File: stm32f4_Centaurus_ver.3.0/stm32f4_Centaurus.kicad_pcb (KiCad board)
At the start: 2 copper layers, 100 x 79 mm, 221 parts, among them IC1 PIC24FJ64GB004, J1 SERIAL1, J2 EXTERNAL_~RST, P1 PICKit3, P10 XA2_12V, P11 CAN0, P12 CAN1, P13 CAN0, P14 CAN1, P15 SERIAL2, P16 SERIAL0, P17 XA2_5V, P18 SWD, P2 SERIAL5_SBDBT, P23 A/D, P24 PWM, P25 A/D_batt, P26 PWM_batt, P27 EMERGENCY_CHECK, P28 I/O_5V, P29 I/O_Variable, P3 ENC0, P30 I/O_5V_batt, P31 I/O_Variable, P4 ENC2, P5 SPI0, P6 ENC3, P7 ENC1, P8 SERIAL4, P9 SERIAL3, Q1 FET_P, Q2 FET_P, Q3 FET_P, Q4 NPN, Q5 NPN, Q6 FET_P, Q7 FET_N, SW1 Main_POWER, SW2 SW1, SW3 SW0, SW4 SW2, SW5 SW3, U1 STM32F407VG, U10 LOGO, U11 TLP4227G-2, U13 LOGO, U2 AZ1086H, U3 MCP2221A, U4 BD9G101G, U5 MAX3051, U6 MAX3051, U7 AQM1602_BL, U8 OSTBABS4C2B, U9 LOGO, X1 8MHz

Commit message: いろいろ修正した(なにやったけ? <-おい)
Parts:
- added Q8: FET_N, Mizz_lib:SOT-23, F.Cu at (145.6, 71.2)
- added R77: 510, Mizz_lib:1608_WP, F.Cu at (146.3, 76.8)
- added R78: 10, Mizz_lib:1608_WP, B.Cu at (117.1, 75.2)
- added R79: 10, Mizz_lib:1608_WP, B.Cu at (117.1, 73.2)
- added R80: 10, Mizz_lib:1608_WP, B.Cu at (114.9, 97.5)
- R76: value 10k -> R_JP; moved to B.Cu
- SP1: footprint Mizz_lib:UGCT7525AN4 -> Mizz_lib:PKLCS1212E4001
- U11: value TLP4227G-2 -> CPC1106N; footprint Package_DIP:DIP-8_W7.62mm_SMDSocket_SmallPads -> Package_SO:SOP-4_3.8x4.1mm_P2.54mm; moved to B.Cu
- moved U11 62.9 mm to (144.3, 76.0), turned to 270 degrees
- moved R76 32.6 mm to (146.4, 68.1), turned to 90 degrees
- moved R64 30.3 mm to (145.6, 73.6), turned to 180 degrees
- moved JP6 3.08 mm to (150.0, 80.2), turned to 270 degrees
- moved SP1 1.25 mm to (80.2, 103.2)
- moved J2 0.45 mm to (140.6, 73.8)
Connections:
- D20 pad 2: +3V3 -> +12V
- D34 pad 1: /PE8 -> /PE12
- JP6 pad 2: Net-(JP6-Pad2) -> /EXTERNAL_~RST~_PIN
- P5 pad 3: /SPI2_MOSI -> Net-(P5-Pad3)
- P5 pad 4: /SPI2_MISO -> Net-(P5-Pad4)
- P5 pad 5: /SPI2_SCK -> Net-(P5-Pad5)
- P5 pad 6: /PE10 -> /PE8
- R17 pad 1: /PE12 -> /PE10
- R64 pad 1: Net-(R64-Pad1) -> Net-(JP6-Pad1)
- R76 pad 1: GND -> Net-(Q8-Pad3)
- R76 pad 2: Net-(R76-Pad2) -> +3V3
- SP1 pad 1: +3V3 -> +12V
- U11 pad 1: Net-(J2-Pad3) -> /ST-LINK_Vdd
- U11 pad 2: Net-(R76-Pad2) -> Net-(R77-Pad2)
- U11 pad 3: /ST-LINK_Vdd -> /~RST
- U11 pad 4: Net-(R64-Pad1) -> /EXTERNAL_~RST~_PIN
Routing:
- net Net-(P5-Pad4): track 0.00 -> 47.5 mm, vias 0 -> 7
- net Net-(P5-Pad3): track 0.00 -> 43.9 mm, vias 0 -> 7
- net Net-(R62-Pad1): track 39.8 -> 0.00 mm, vias 7 -> 0
- net Net-(R64-Pad2): track 39.2 -> 0.00 mm, vias 7 -> 0
- net /~RST: track 67.9 -> 94.8 mm
- net Net-(P5-Pad5): track 0.00 -> 26.5 mm
- net +12V: track 25.9 -> 43.1 mm, vias 2 -> 3
- net /PE12: track 23.3 -> 36.6 mm, vias 3 -> 2
- net /PE15: track 53.0 -> 65.8 mm
- net Net-(JP6-Pad1): track 1.21 -> 11.4 mm, vias 0 -> 1
- net /PE10: track 33.9 -> 42.8 mm, vias 2 -> 4
- net +3V3: track 397.1 -> 389.4 mm, vias 25 -> 23
- net /SWCLK: track 29.1 -> 35.9 mm
- net /EXTERNAL_~RST~_PIN: track 0.00 -> 6.68 mm
- net Net-(R63-Pad2): track 6.31 -> 0.00 mm
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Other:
- board text added: "CS_PE8"
- board text removed: "CS"

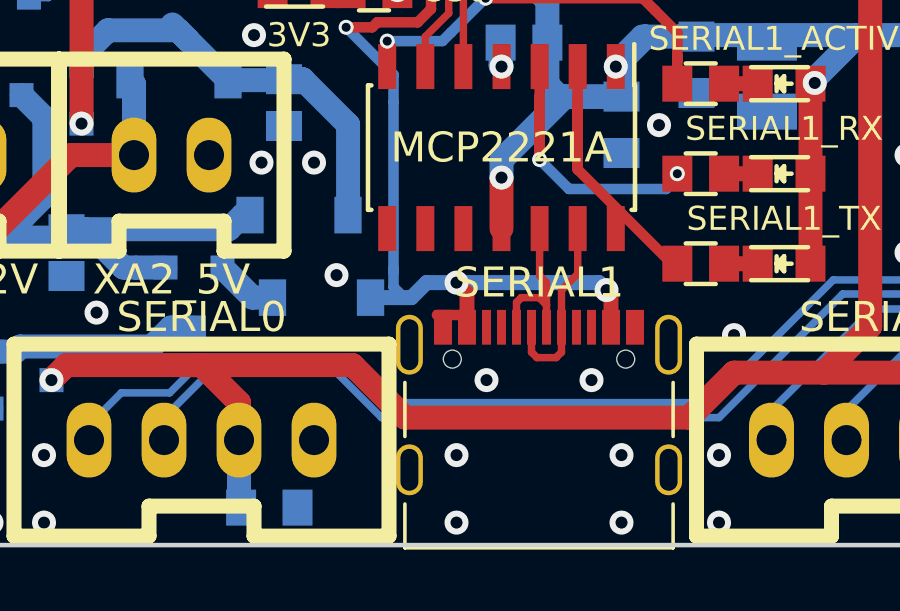
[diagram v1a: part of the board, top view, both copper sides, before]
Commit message: BLDC type2引き終わった，基板にミスがあった
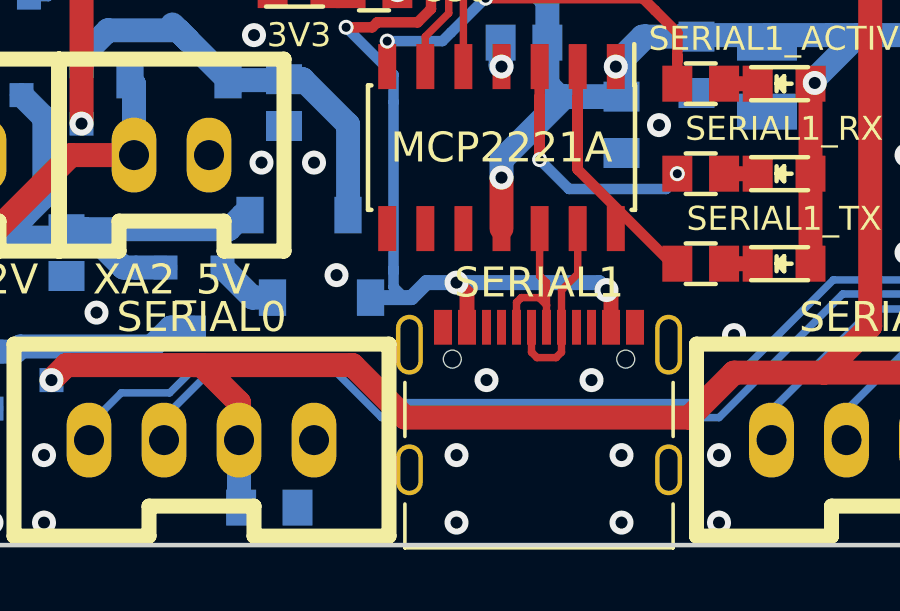
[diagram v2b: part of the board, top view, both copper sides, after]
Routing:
- net /BUS_5V: track 29.3 -> 28.5 mm
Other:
- board text added: "STM32F407VGT6 Board "Centaurus" ver.3.0"
- board text removed: "STM32F407VGT6 Board "Centaurus" ver.2.1.1"

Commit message: またまたミス発見，直した
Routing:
- net Net-(D25-Pad2): track 0.00 -> 0.09 mm, vias 0 -> 1
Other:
- board text added: "11"
- board text removed: "7(RGB,RESET)"
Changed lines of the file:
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@@
     (thickness 1.6)
     (drawings 150)
-    (tracks 2855)
+    (tracks 2857)
     (zones 0)
     (modules 226)
@@
     (effects (font (size 0.8 0.8) (thickness 0.2)) (justify mirror))
   )
-  (gr_text "7(RGB,RESET)" (at 76.5 72.25) (layer B.SilkS)
+  (gr_text 11 (at 76.5 72.25) (layer B.SilkS)
     (effects (font (size 0.8 0.8) (thickness 0.2)) (justify mirror))
   )
@@
   (via (at 112.25 115.63) (size 0.5) (drill 0.3) (layers F.Cu B.Cu) (net 165))
   (segment (start 112.25 115.72) (end 112.25 115.63) (width 0.25) (layer B.Cu) (net 165))
+  (via (at 117.95 115.72) (size 0.5) (drill 0.3) (layers F.Cu B.Cu) (net 166))
+  (segment (start 117.95 115.63) (end 117.95 115.72) (width 0.25) (layer F.Cu) (net 166))
   (segment (start 58.25 73.21) (end 57.29 72.25) (width 0.5) (layer B.Cu) (net 167))
   (segment (start 58.25 81.72) (end 58.25 73.21) (width 0.5) (layer B.Cu) (net 167))

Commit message: 卍配　置　完　了卍
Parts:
- removed Q8: FET_N, Mizz_lib:SOT-23
- added U12: PS7200K-1A, Package_SO:SOP-4_3.8x4.1mm_P2.54mm, B.Cu at (133.2, 74.7)
- R64: moved to B.Cu
- R76: value R_JP -> 330; moved to F.Cu
- moved R76 17.9 mm to (163.8, 72.5), turned to 0 degrees
- moved R64 11.4 mm to (134.4, 71.8)
- moved D40 0.40 mm to (144.2, 71.1)
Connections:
- J2 pad 3: Net-(J2-Pad3) -> /RESET_SIGNAL
- R76 pad 1: Net-(Q8-Pad3) -> GND
- R76 pad 2: +3V3 -> Net-(R76-Pad2)
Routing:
- net Net-(JP6-Pad1): track 11.4 -> 26.3 mm
- net Net-(J2-Pad3): track 5.97 -> 0.00 mm, vias 1 -> 0
- net Net-(Q8-Pad3): track 1.79 -> 0.00 mm, vias 1 -> 0
- net GND: vias 362 -> 360

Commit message: main絶対動くマン
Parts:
- R76: moved to B.Cu
- moved R76 35.6 mm to (128.2, 72.2)
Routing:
- net /RESET_SIGNAL: track 0.00 -> 11.0 mm
- net Net-(R76-Pad2): track 0.00 -> 1.98 mm
- net +3V3: track 389.4 -> 390.7 mm, vias 23 -> 24
- net GND: vias 360 -> 365
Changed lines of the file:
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@@
     (thickness 1.6)
     (drawings 150)
-    (tracks 2857)
+    (tracks 2875)
     (zones 0)
     (modules 226)
@@
       (net 60 "Net-(D20-Pad1)"))
   )
-  (module Mizz_lib:1608_WP (layer F.Cu)
-    (at 163.79 72.5)
+  (module Mizz_lib:1608_WP (layer B.Cu)
+    (at 128.15 72.15)
     (descr <b>CAPACITOR</b>)
-    (fp_text reference R76 (at -0.635 -0.635) (layer F.SilkS) hide
-      (effects (font (size 1.2065 1.2065) (thickness 0.1016)) (justify left bottom))
+    (fp_text reference R76 (at -0.635 0.635) (layer B.SilkS) hide
+      (effects (font (size 1.2065 1.2065) (thickness 0.1016)) (justify right bottom mirror))
     )
-    (fp_text value 330 (at 0 -0.5) (layer F.SilkS)
-      (effects (font (size 0.8 0.8) (thickness 0.15)) (justify bottom))
+    (fp_text value 330 (at -2.7 0.5) (layer B.SilkS)
+      (effects (font (size 0.8 0.8) (thickness 0.15)) (justify bottom mirror))
     )
-    (fp_line (start -0.356 -0.432) (end 0.356 -0.432) (layer Dwgs.User) (width 0.1016))
-    (fp_line (start -0.356 0.419) (end 0.356 0.419) (layer Dwgs.User) (width 0.1016))
-    (fp_poly (pts (xy -0.8382 0.4699) (xy -0.3381 0.4699) (xy -0.3381 -0.4801) (xy -0.8382 -0.4801)) (layer Dwgs.User) (width 0))
-    (fp_poly (pts (xy 0.3302 0.4699) (xy 0.8303 0.4699) (xy 0.8303 -0.4801) (xy 0.3302 -0.4801)) (layer Dwgs.User) (width 0))
-    (fp_poly (pts (xy -0.1999 0.3) (xy 0.1999 0.3) (xy 0.1999 -0.3) (xy -0.1999 -0.3)) (layer F.Adhes) (width 0))
-    (pad 1 smd rect (at -0.9 0) (size 0.8 1) (layers F.Cu F.Paste F.Mask)
+    (fp_line (start -0.356 0.432) (end 0.356 0.432) (layer Dwgs.User) (width 0.1016))
+    (fp_line (start -0.356 -0.419) (end 0.356 -0.419) (layer Dwgs.User) (width 0.1016))
+    (fp_poly (pts (xy -0.8382 -0.4699) (xy -0.3381 -0.4699) (xy -0.3381 0.4801) (xy -0.8382 0.4801)) (layer Dwgs.User) (width 0))
+    (fp_poly (pts (xy 0.3302 -0.4699) (xy 0.8303 -0.4699) (xy 0.8303 0.4801) (xy 0.3302 0.4801)) (layer Dwgs.User) (width 0))
+    (fp_poly (pts (xy -0.1999 -0.3) (xy 0.1999 -0.3) (xy 0.1999 0.3) (xy -0.1999 0.3)) (layer B.Adhes) (width 0))
+    (pad 1 smd rect (at -0.9 0) (size 0.8 1) (layers B.Cu B.Paste B.Mask)
       (net 2 GND))
-    (pad 2 smd rect (at 0.9 0) (size 0.8 1) (layers F.Cu F.Paste F.Mask)
+    (pad 2 smd rect (at 0.9 0) (size 0.8 1) (layers B.Cu B.Paste B.Mask)
       (net 230 "Net-(R76-Pad2)"))
     (model ${KISYS3DMOD}/Resistor_SMD.3dshapes/R_0603_1608Metric.step
@@
   (via (at 141.25 132.25) (size 0.8) (drill 0.4) (layers F.Cu B.Cu) (net 2))
   (via (at 137.5 82.75) (size 0.8) (drill 0.4) (layers F.Cu B.Cu) (net 2))
-  (via (at 137.75 75) (size 0.8) (drill 0.4) (layers F.Cu B.Cu) (net 2))
   (via (at 144.675 74.575) (size 0.5) (drill 0.3) (layers F.Cu B.Cu) (net 2))
   (via (at 140.6 81.175) (size 0.8) (drill 0.4) (layers F.Cu B.Cu) (net 2))
@@
   (via (at 112.85 103.65) (size 0.8) (drill 0.4) (layers F.Cu B.Cu) (net 2))
   (via (at 110.6 107.4) (size 0.8) (drill 0.4) (layers F.Cu B.Cu) (net 2))
+  (via (at 137.7 75.1) (size 0.8) (drill 0.4) (layers F.Cu B.Cu) (net 2))
+  (via (at 134.95 76.7) (size 0.8) (drill 0.4) (layers F.Cu B.Cu) (net 2))
+  (via (at 132.85 69.95) (size 0.5) (drill 0.3) (layers F.Cu B.Cu) (net 2))
+  (via (at 134.25 70.45) (size 0.5) (drill 0.3) (layers F.Cu B.Cu) (net 2))
+  (via (at 134.8 72.85) (size 0.8) (drill 0.4) (layers F.Cu B.Cu) (net 2))
+  (via (at 134.8 75.05) (size 0.8) (drill 0.4) (layers F.Cu B.Cu) (net 2))
   (segment (start 149.42 124.21) (end 148.49 124.21) (width 0.25) (layer B.Cu) (net 3))
   (segment (start 148.49 124.21) (end 148.275001 124.424999) (width 0.25) (layer B.Cu) (net 3))
@@
   (via (at 137 71.75) (size 0.8) (drill 0.4) (layers F.Cu B.Cu) (net 212))
   (segment (start 136.64 72.11) (end 137 71.75) (width 0.8) (layer F.Cu) (net 212))
-  (segment (start 136.64 81.14) (end 136.64 72.11) (width 0.8) (layer F.Cu) (net 212))
   (segment (start 135.83 81.95) (end 136.64 81.14) (width 0.8) (layer F.Cu) (net 212))
   (segment (start 137 71.75) (end 139.915 71.75) (width 0.8) (layer B.Cu) (net 212))
@@
   (segment (start 146.04 66.79) (end 146.45 67.2) (width 0.35) (layer B.Cu) (net 212))
   (segment (start 144.25 66.79) (end 146.04 66.79) (width 0.35) (layer B.Cu) (net 212))
+  (segment (start 136 75.6) (end 136.65 74.95) (width 0.35) (layer B.Cu) (net 212))
+  (via (at 136.65 74.95) (size 0.8) (drill 0.4) (layers F.Cu B.Cu) (net 212))
+  (segment (start 136 75.97) (end 136 75.6) (width 0.35) (layer B.Cu) (net 212))
+  (segment (start 136.64 81.14) (end 136.65 74.95) (width 0.8) (layer F.Cu) (net 212))
+  (segment (start 136.65 74.95) (end 136.64 72.11) (width 0.8) (layer F.Cu) (net 212))
   (via (at 126.89 78.83) (size 0.5) (drill 0.3) (layers F.Cu B.Cu) (net 218))
   (segment (start 127.5 79.44) (end 126.89 78.83) (width 0.25) (layer F.Cu) (net 218))
@@
   (segment (start 98.25 103.325) (end 98.25 105.75) (width 0.25) (layer F.Cu) (net 228))
   (segment (start 98.875 102.7) (end 98.25 103.325) (width 0.25) (layer F.Cu) (net 228))
+  (segment (start 136.986001 74.249999) (end 134.400001 74.249999) (width 0.2) (layer B.Cu) (net 229))
+  (segment (start 137.036002 74.3) (end 136.986001 74.249999) (width 0.2) (layer B.Cu) (net 229))
+  (segment (start 138.55 74.3) (end 137.036002 74.3) (width 0.2) (layer B.Cu) (net 229))
+  (segment (start 140.55 73.75) (end 139.1 73.75) (width 0.2) (layer B.Cu) (net 229))
+  (segment (start 139.1 73.75) (end 138.55 74.3) (width 0.2) (layer B.Cu) (net 229))
+  (segment (start 132.68 75.97) (end 130.5 75.97) (width 0.2) (layer B.Cu) (net 229))
+  (segment (start 134.400001 74.249999) (end 132.68 75.97) (width 0.2) (layer B.Cu) (net 229))
+  (segment (start 130.33 73.43) (end 129.05 72.15) (width 0.35) (layer B.Cu) (net 230))
+  (segment (start 130.5 73.43) (end 130.33 73.43) (width 0.35) (layer B.Cu) (net 230))
   (zone (net 2) (net_name GND) (layer F.Cu) (hatch edge 0.508)
     (connect_pads yes (clearance 0.2))

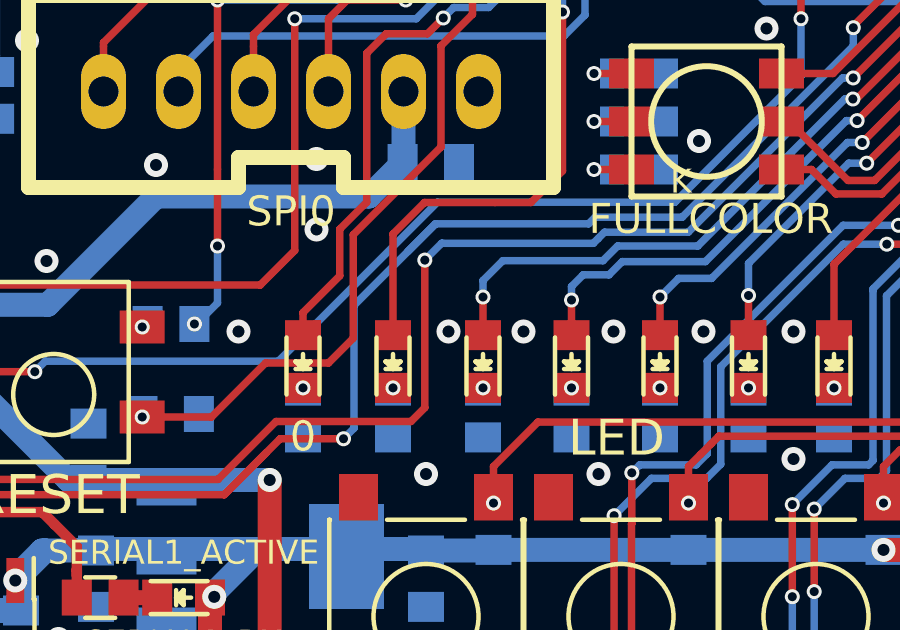
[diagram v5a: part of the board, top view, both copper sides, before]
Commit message: メイン基板，ビア改良
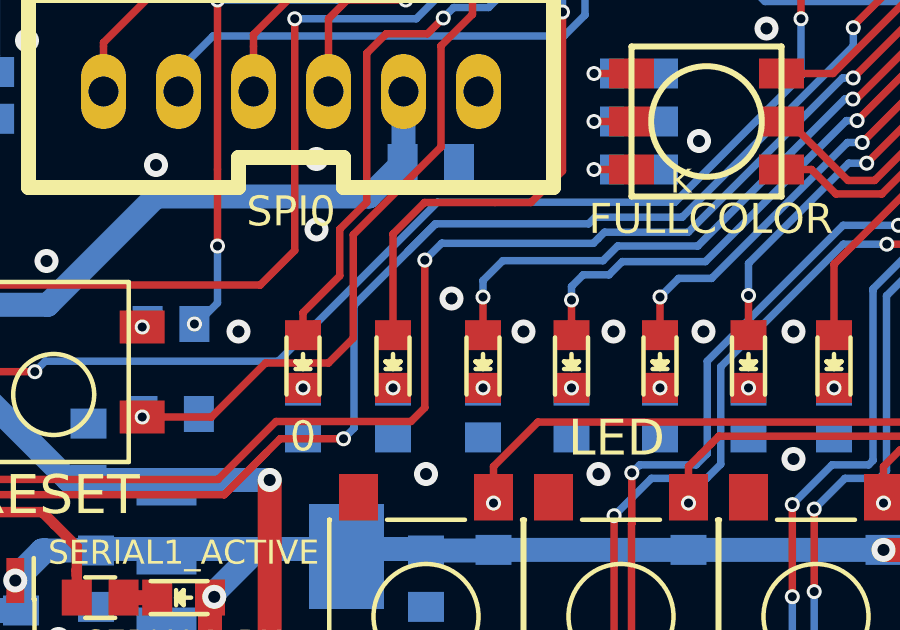
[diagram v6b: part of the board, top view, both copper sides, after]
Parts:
- R64: value 10k -> 4.7k
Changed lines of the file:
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@@
   )
   (setup
-    (last_trace_width 0.2)
+    (last_trace_width 0.25)
     (user_trace_width 0.2)
     (user_trace_width 0.35)
@@
       (drillshape 0)
       (scaleselection 1)
-      (outputdirectory "加工データ/"))
+      (outputdirectory "C:/Users/3Zuta/Documents/NHK_RC20_PCBs/stm32f4_Centaurus_ver.3.0/加工データ/"))
   )
   (net 0 "")
@@
       (effects (font (size 1.2065 1.2065) (thickness 0.1016)) (justify left bottom mirror))
     )
-    (fp_text value 10k (at 2.55 -0.45) (layer B.SilkS)
+    (fp_text value 4.7k (at 2.75 -0.45) (layer B.SilkS)
       (effects (font (size 0.8 0.8) (thickness 0.15)) (justify bottom mirror))
     )
@@
   (via (at 101.5 118.5) (size 0.8) (drill 0.4) (layers F.Cu B.Cu) (net 2))
   (via (at 107.25 118.5) (size 0.8) (drill 0.4) (layers F.Cu B.Cu) (net 2))
-  (via (at 102.25 113.75) (size 0.8) (drill 0.4) (layers F.Cu B.Cu) (net 2))
+  (via (at 102.35 112.65) (size 0.8) (drill 0.4) (layers F.Cu B.Cu) (net 2))
   (via (at 104.75 113.75) (size 0.8) (drill 0.4) (layers F.Cu B.Cu) (net 2))
   (via (at 107.75 113.75) (size 0.8) (drill 0.4) (layers F.Cu B.Cu) (net 2))
